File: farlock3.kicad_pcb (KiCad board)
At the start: 2 copper layers, 53 x 17.8 mm, 38 parts, among them J1 USB_B_Micro, J2 Conn_01x17, SW1 SW_SPDT, U1 MDBT50Q, U2 MX25R6435FZNIL0, U3 TB6612FNG, U4 AP2112K-3.3, Y1 32.768kHz

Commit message: v02 redesign
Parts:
- added C12: 10µF, Capacitor_SMD:C_0603_1608Metric, F.Cu at (155.6, 85.1)
- added C13: 0.1µF, Capacitor_SMD:C_0603_1608Metric, F.Cu at (155.3, 83.3)
- added D3: PRTR5V0U2X, Package_TO_SOT_SMD:SOT-143, F.Cu at (158.9, 84.1)
- added J3: Conn_01x02, Connector_PinHeader_2.54mm:PinHeader_1x02_P2.54mm_Vertical, F.Cu at (180.0, 88.4)
- added J4: Conn_01x02, Connector_PinHeader_2.54mm:PinHeader_1x02_P2.54mm_Vertical, F.Cu at (154.4, 93.1)
- added J5: Conn_01x10, Connector_PinHeader_2.54mm:PinHeader_1x10_P2.54mm_Vertical, F.Cu at (128.3, 76.9)
- added J6: Conn_01x03, Connector_PinHeader_2.54mm:PinHeader_1x03_P2.54mm_Vertical, F.Cu at (169.9, 95.6)
- added R10: 330, Resistor_SMD:R_0603_1608Metric, F.Cu at (180.9, 95.2)
- added R4: 10k, Resistor_SMD:R_0603_1608Metric, F.Cu at (129.3, 80.3)
- added R5: 10k, Resistor_SMD:R_0603_1608Metric, F.Cu at (178.2, 94.8)
- J2: value Conn_01x17 -> Conn_01x05; footprint Connector_PinHeader_2.54mm:PinHeader_1x17_P2.54mm_Vertical -> Connector_PinHeader_2.54mm:PinHeader_1x05_P2.54mm_Vertical
- SW1: footprint Button_Switch_SMD:SW_SPDT_PCM12 -> OS102011MA1QN1:OS102011MA1QN1
- U1: footprint MDBT50Q:MDBT50Q -> MDBT50Q:MDBT50Q-U1M
- moved J1 65.0 mm to (158.6, 79.7), turned to 180 degrees
- moved R2 62.8 mm to (169.8, 88.8)
- moved R9 62.1 mm to (147.0, 80.1), turned to 180 degrees
- moved R8 61.4 mm to (151.2, 80.4), turned to 90 degrees
- moved R1 61.4 mm to (169.1, 87.3)
- moved C8 56.9 mm to (138.0, 82.8), turned to 180 degrees
- moved C14 55.7 mm to (147.7, 95.2), turned to 90 degrees
- moved D5 54.7 mm to (148.6, 85.8), turned to 90 degrees
- moved C17 53.8 mm to (150.9, 91.6), turned to -90 degrees
- moved JP1 52.9 mm to (150.3, 85.8), turned to 0 degrees
- moved R6 52.9 mm to (150.3, 85.8), turned to 90 degrees
- moved C4 52.8 mm to (164.7, 76.7)
- moved C15 52.7 mm to (147.7, 91.6), turned to -90 degrees
- moved C9 52.6 mm to (134.5, 85.7), turned to 180 degrees
- moved Y1 52.3 mm to (166.6, 77.2)
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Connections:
- net D+_CON renamed D+
- net D-_CON renamed D-
- C1 pad 2: SW_POS2 -> GND
- C10 pad 2: SW_POS2 -> GND
- C11 pad 2: SW_POS2 -> GND
- C14 pad 2: SW_POS2 -> GND
- C15 pad 2: SW_POS2 -> GND
- C16 pad 2: SW_POS2 -> GND
- C17 pad 2: SW_POS2 -> GND
- C2 pad 2: SW_POS2 -> GND
- C3 pad 2: SW_POS2 -> GND
- C4 pad 2: SW_POS2 -> GND
- C5 pad 2: SW_POS2 -> GND
- C6 pad 2: SW_POS2 -> GND
- C7 pad 2: SW_POS2 -> GND
- C8 pad 2: SW_POS2 -> GND
- C9 pad 2: SW_POS2 -> GND
- J1 pad 5: SW_POS2 -> GND
- J1 pad 6: SW_POS2 -> GND
- J2 pad 1: VIN -> SWDIO
- J2 pad 2: SW_POS2 -> SWDCLK
- J2 pad 3: +3V3 -> RESET
- J2 pad 4: MOTOR_1 -> GND
- J2 pad 5: MOTOR_2 -> +3V3
- JP1 pad 1: SW_POS2 -> GND
- R7 pad 1: P0.25 -> P0.24
- SW1 pad 1: SW_POS2 -> unconnected-(SW1-A-Pad1)
- SW1 pad 2: Net-(SW1-B) -> P0.24
- SW1 pad 3: +VDC -> GND
- U1 pad 1: SW_POS2 -> GND
- U1 pad 15: SW_POS2 -> GND
- U1 pad 2: SW_POS2 -> GND
- U1 pad 29: unconnected-(U1-P0.12-Pad29) -> P0.12
- U1 pad 33: SW_POS2 -> GND
- U1 pad 36: unconnected-(U1-P0.14-Pad36) -> LED_CXN-
- U1 pad 48: unconnected-(U1-P0.24-Pad48) -> P0.24
- U1 pad 55: SW_POS2 -> GND
- U2 pad 4: SW_POS2 -> GND
- U3 pad 10: SW_POS2 -> GND
- U3 pad 18: SW_POS2 -> GND
- U3 pad 3: SW_POS2 -> GND
- U3 pad 4: SW_POS2 -> GND
- U3 pad 9: SW_POS2 -> GND
- U4 pad 2: SW_POS2 -> GND
- U4 pad 3: Net-(SW1-B) -> +VDC
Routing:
- net LED_ACCD-: track 13.1 -> 81.1 mm
- net Net-(U1-D-): track 65.5 -> 1.84 mm, vias 2 -> 0
- net LED_ACCG-: track 6.80 -> 69.0 mm
- net +3V3: track 70.6 -> 130.6 mm, vias 4 -> 5
- net SWDCLK: track 23.0 -> 78.5 mm
- net Net-(U1-D+): track 58.2 -> 3.44 mm, vias 2 -> 0
- net RESET: track 18.9 -> 72.7 mm
- net P0.25: track 30.5 -> 79.2 mm, vias 4 -> 1
- net P0.24: track 0.00 -> 48.4 mm
- net SWDIO: track 24.9 -> 72.8 mm
- net P0.09/NFC1: track 17.1 -> 62.0 mm, vias 1 -> 0
- net P0.10/NFC2: track 17.2 -> 61.6 mm, vias 2 -> 0
- net P0.12: track 0.00 -> 30.2 mm, vias 0 -> 2
- net P0.23: track 26.8 -> 8.63 mm
- net P0.19: track 22.9 -> 4.85 mm, vias 2 -> 0
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- added copper zone on B.Cu, net GND
- added copper zone on F.Cu, net GND
- removed copper zone on F.Cu, net +VDC
- removed copper zone on B.Cu, net SW_POS2
- removed copper zone on F.Cu, net SW_POS2
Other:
- board size 53 x 17.8 mm -> 58 x 22.5 mm
- board text added: "farlock3 v02"
- board text removed: "farlock3 v01"

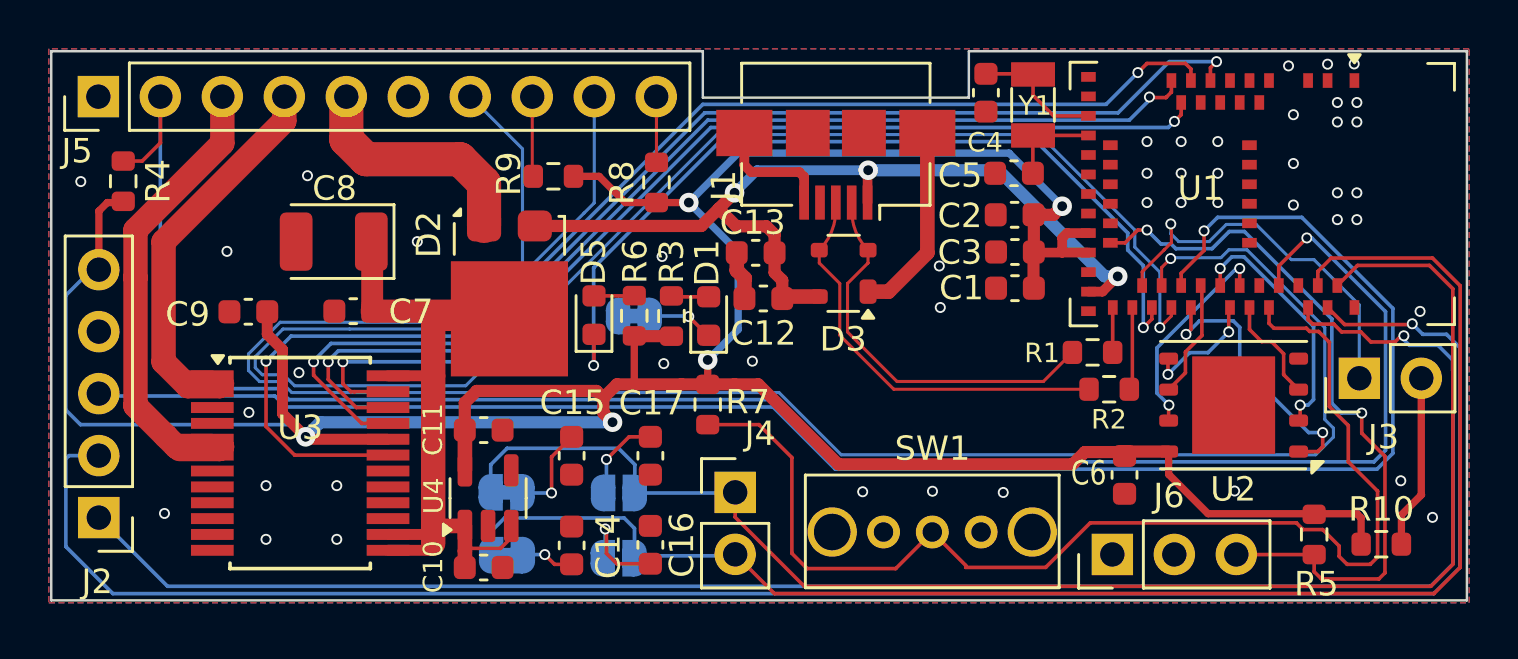
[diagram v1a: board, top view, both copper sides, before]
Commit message: increase minimum track width, spacing, and annular ring size - support more board fabrication houses
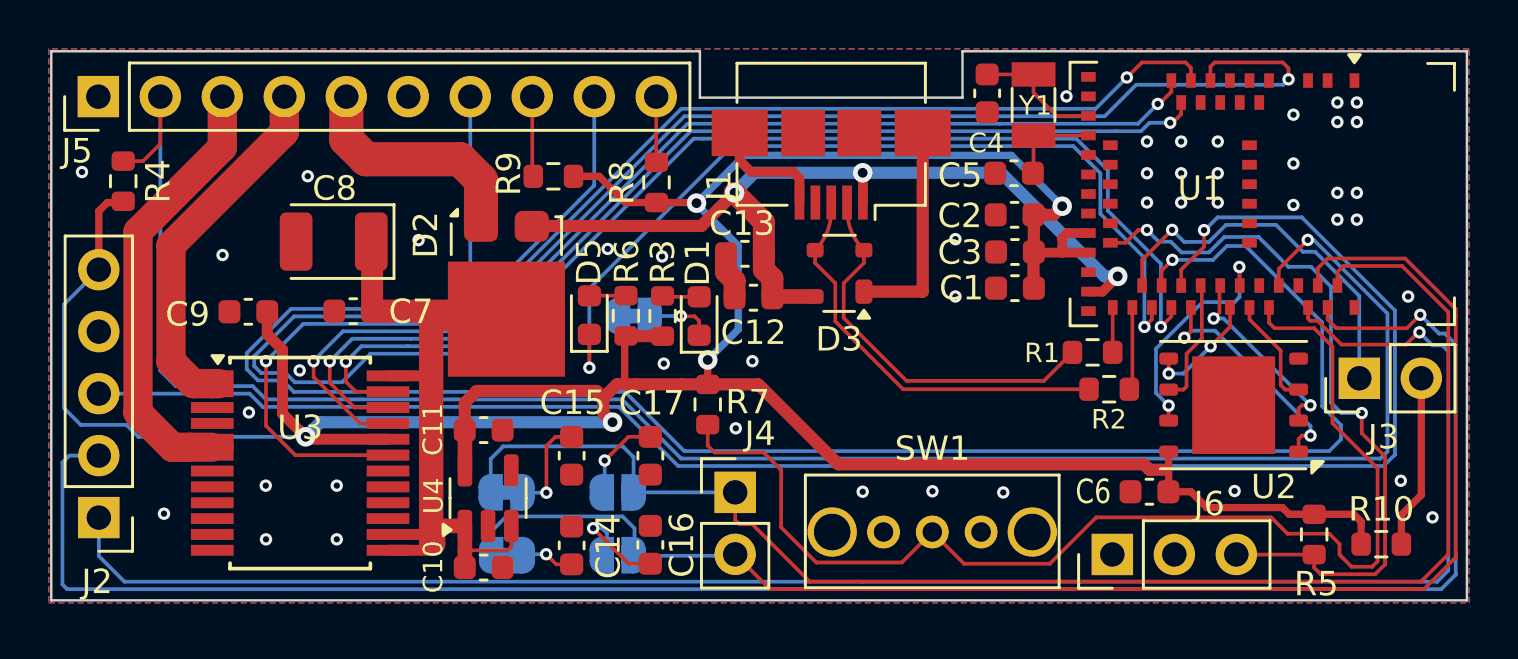
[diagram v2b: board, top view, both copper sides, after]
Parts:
- moved C6 1.23 mm to (171.4, 93.0), turned to 180 degrees
- moved C13 0.44 mm to (154.8, 83.3)
- moved C12 0.41 mm to (155.2, 85.1)
- moved D1 0.39 mm to (152.9, 85.8)
- moved R3 0.37 mm to (151.4, 85.8)
- moved R6 0.34 mm to (149.9, 85.8)
- moved D5 0.19 mm to (148.4, 85.8)
- moved J1 0.19 mm to (158.4, 79.7)
- moved D3 0.17 mm to (158.7, 84.1)
- moved JP5 0.13 mm to (149.6, 95.7)
- moved D2 0.13 mm to (145.1, 84.9)
- moved C4 0.06 mm to (164.8, 76.7)
- moved JP4 0.06 mm to (149.6, 93.1)
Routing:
- net P0.29: track 47.4 -> 53.6 mm
- net P0.21: track 10.3 -> 7.90 mm
- net P0.17: track 11.5 -> 9.71 mm
- net LED_ACCD-: track 81.1 -> 79.5 mm
- net SWDCLK: track 78.5 -> 80.1 mm
- net MOTOR_2: track 22.7 -> 24.2 mm
- net P0.09/NFC1: track 62.0 -> 60.8 mm
- net MOTOR_1: track 19.1 -> 18.1 mm
- net P0.23: track 8.63 -> 9.50 mm
- net SWDIO: track 72.8 -> 73.7 mm
- net GND: track 15.0 -> 15.7 mm, vias 42 -> 46
- net P0.10/NFC2: track 61.6 -> 61.0 mm
- net VBUS: track 36.5 -> 35.9 mm
- net (no net): vias 4 -> 0
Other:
- outline, holes or cut-outs redrawn
- rule pad_to_mask_clearance: 0 -> 0.0508
